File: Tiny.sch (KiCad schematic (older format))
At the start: 7 parts, among them IC601 MAX6126AASA25+

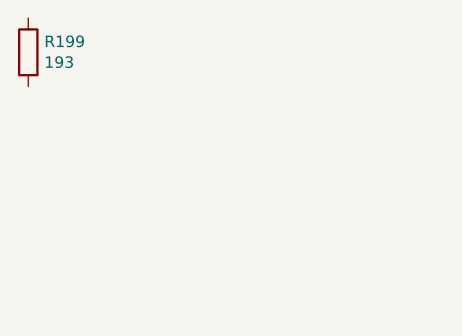
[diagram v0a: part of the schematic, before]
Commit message: added new kicad_mod libs to footprint libraries
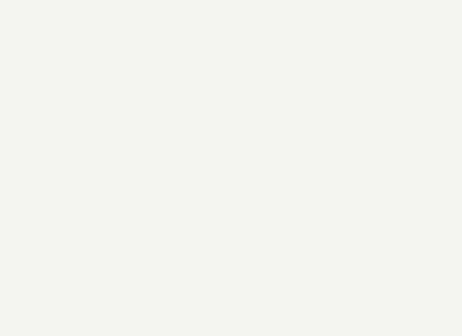
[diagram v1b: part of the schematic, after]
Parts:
- removed R199: 193, symbol Device:R
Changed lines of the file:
@@
 Wire Wire Line
 	5400 4500 5400 4600
-$Comp
-L Device:R R199
-U 1 1 60CC9952
-P 3650 2300
-F 0 "R199" H 3720 2346 50  0000 L CNN
-F 1 "193" H 3720 2255 50  0000 L CNN
-F 2 "" V 3580 2300 50  0001 C CNN
-F 3 "~" H 3650 2300 50  0001 C CNN
-	1    3650 2300
-	1    0    0    -1
-$EndComp
 $EndSCHEMATC

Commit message: add footprints julia
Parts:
- IC601: footprint SOIC127P600X175-8N -> footprint libraries:MAX6126-25+
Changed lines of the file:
@@
 F 0 "IC601" H 6350 4265 50  0000 C CNN
 F 1 "MAX6126AASA25+" H 6350 4174 50  0000 C CNN
-F 2 "SOIC127P600X175-8N" H 6750 4100 50  0001 L CNN
+F 2 "footprint libraries:MAX6126-25+" H 6750 4100 50  0001 L CNN
 F 3 "http://datasheets.maximintegrated.com/en/ds/MAX6126.pdf" H 6750 4000 50  0001 L CNN
 F 4 "MAX6126AASA25+, Precision Voltage Reference 0.02% 10mA 12.6V max. 8-Pin SO" H 6750 3900 50  0001 L CNN "Description"

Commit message: added vishay dude & capacitor & resistor footprints
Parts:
- C601, C602, C603, C604, C605: footprint (none) -> Capacitor_SMD:C_0402_1005Metric
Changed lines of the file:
@@
 F 0 "C605" H 7165 4396 50  0000 L CNN
 F 1 "0.1u" H 7165 4305 50  0000 L CNN
-F 2 "" H 7088 4200 50  0001 C CNN
+F 2 "Capacitor_SMD:C_0402_1005Metric" H 7088 4200 50  0001 C CNN
 F 3 "~" H 7050 4350 50  0001 C CNN
 	1    7050 4350
@@
 F 0 "C603" H 5335 3846 50  0000 R CNN
 F 1 "0.1u" H 5335 3755 50  0000 R CNN
-F 2 "" H 5488 3650 50  0001 C CNN
+F 2 "Capacitor_SMD:C_0402_1005Metric" H 5488 3650 50  0001 C CNN
 F 3 "~" H 5450 3800 50  0001 C CNN
 	1    5450 3800
@@
 F 0 "C601" H 4735 4296 50  0000 R CNN
 F 1 "0.1u" H 4735 4205 50  0000 R CNN
-F 2 "" H 4888 4100 50  0001 C CNN
+F 2 "Capacitor_SMD:C_0402_1005Metric" H 4888 4100 50  0001 C CNN
 F 3 "~" H 4850 4250 50  0001 C CNN
 	1    4850 4250
@@
 F 0 "C602" H 5100 4400 50  0000 R CNN
 F 1 "0.1u" H 5150 4300 50  0000 R CNN
-F 2 "" H 5288 4200 50  0001 C CNN
+F 2 "Capacitor_SMD:C_0402_1005Metric" H 5288 4200 50  0001 C CNN
 F 3 "~" H 5250 4350 50  0001 C CNN
 	1    5250 4350
@@
 F 0 "C604" H 5450 4400 50  0000 R CNN
 F 1 "1u" H 5450 4300 50  0000 R CNN
-F 2 "" H 5588 4200 50  0001 C CNN
+F 2 "Capacitor_SMD:C_0402_1005Metric" H 5588 4200 50  0001 C CNN
 F 3 "~" H 5550 4350 50  0001 C CNN
 	1    5550 4350

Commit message: pushing all changes and ports
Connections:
- net POWER_3.3V renamed 3.3V
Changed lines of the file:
@@
 Wire Wire Line
 	7050 4200 7400 4200
-Text GLabel 7400 4200 2    50   Input ~ 0
+Text GLabel 7400 4200 2    50   Output ~ 0
 REFERENCE_2.5V
 $Comp
@@
 	4850 4100 4650 4100
 Connection ~ 4850 4100
-Text Label 4650 4100 2    50   ~ 0
-POWER_3.3V
 Wire Wire Line
 	5400 4100 5400 4200
@@
 Wire Wire Line
 	5750 4300 5750 4600
-$Comp
-L power:GND #PWR0602
-U 1 1 60DBD2AA
-P 5400 4600
-F 0 "#PWR0602" H 5400 4350 50  0001 C CNN
-F 1 "GND" H 5405 4427 50  0000 C CNN
-F 2 "" H 5400 4600 50  0001 C CNN
-F 3 "" H 5400 4600 50  0001 C CNN
-	1    5400 4600
-	1    0    0    -1
-$EndComp
 Wire Wire Line
 	5400 4500 5400 4600
+Text GLabel 4650 4100 0    50   Input ~ 0
+3.3V
+Wire Wire Line
+	5400 4600 5700 4600
+Wire Wire Line
+	5700 4600 5700 4200
+Wire Wire Line
+	5700 4200 5750 4200
+Connection ~ 5750 4200
 $EndSCHEMATC
